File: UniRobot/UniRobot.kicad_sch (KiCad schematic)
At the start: 6 parts, among them J1 Conn_01x01_Socket, J2 Conn_01x01_Socket, Q1 BSS138, U1 RFM69HW

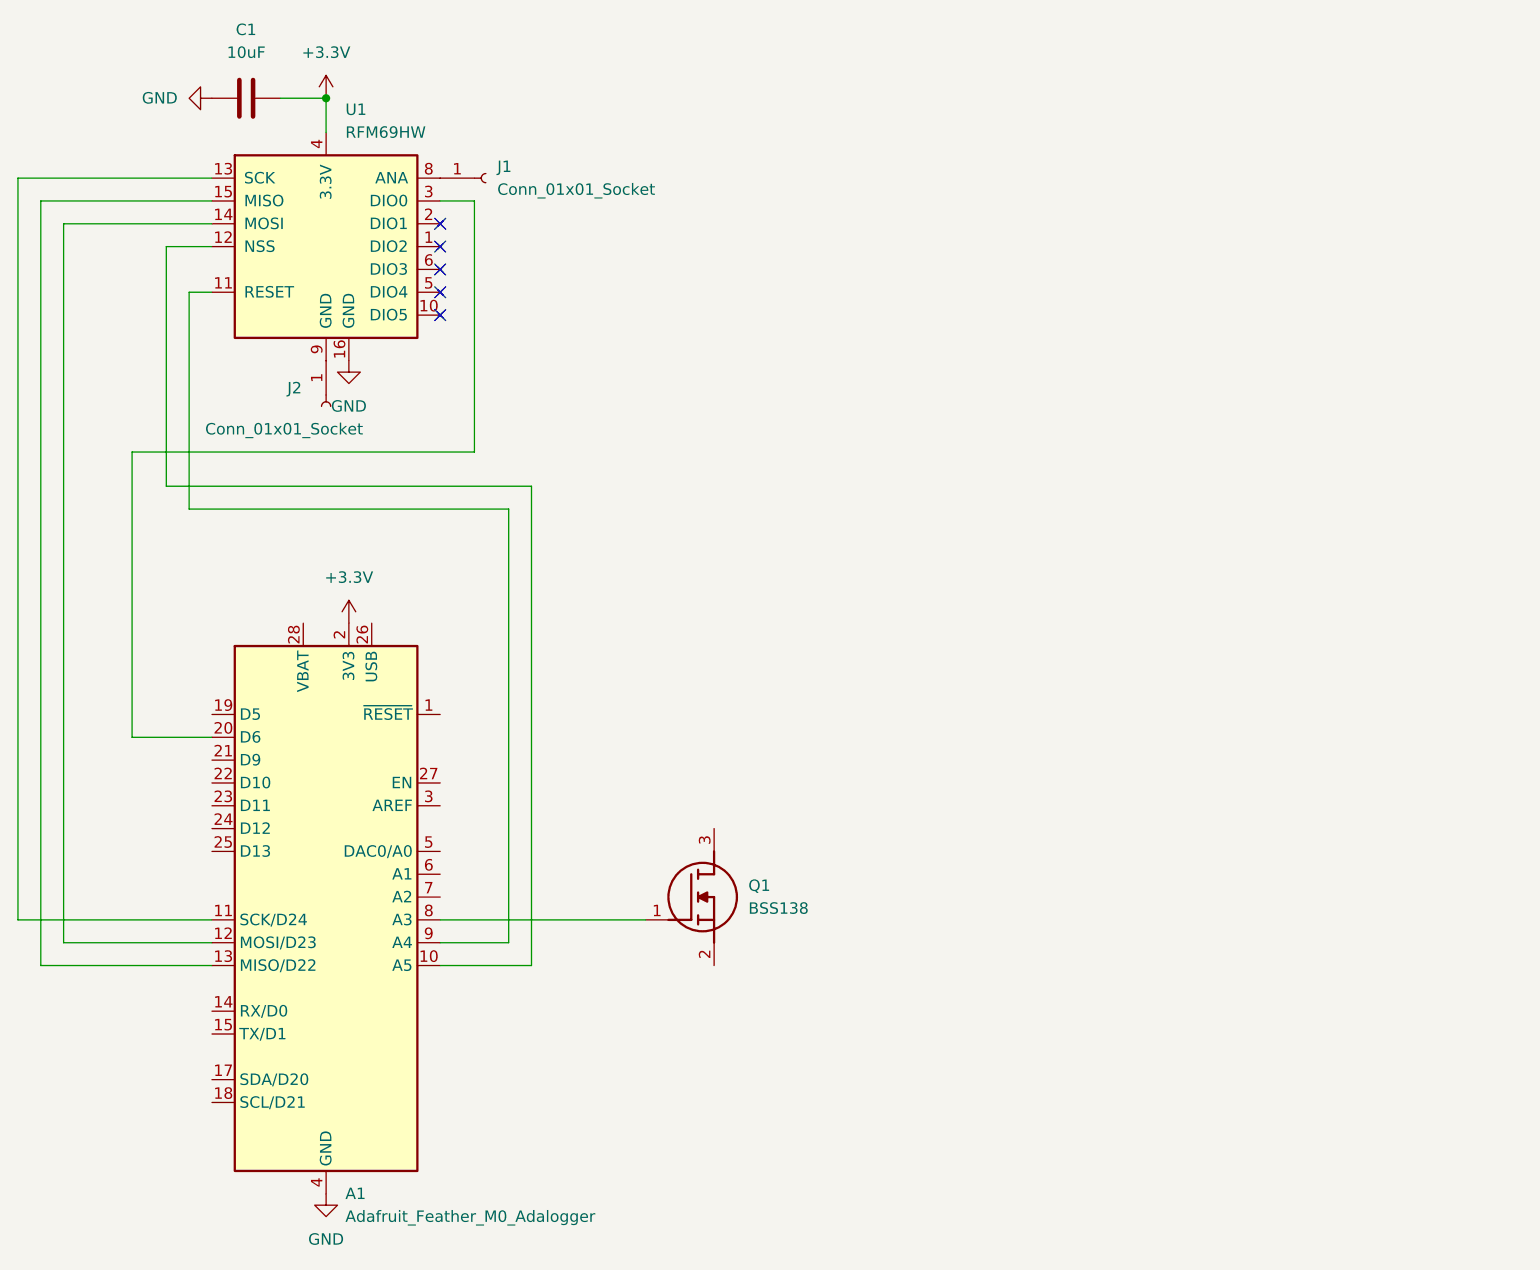
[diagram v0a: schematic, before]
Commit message: lavede robot side pcb.
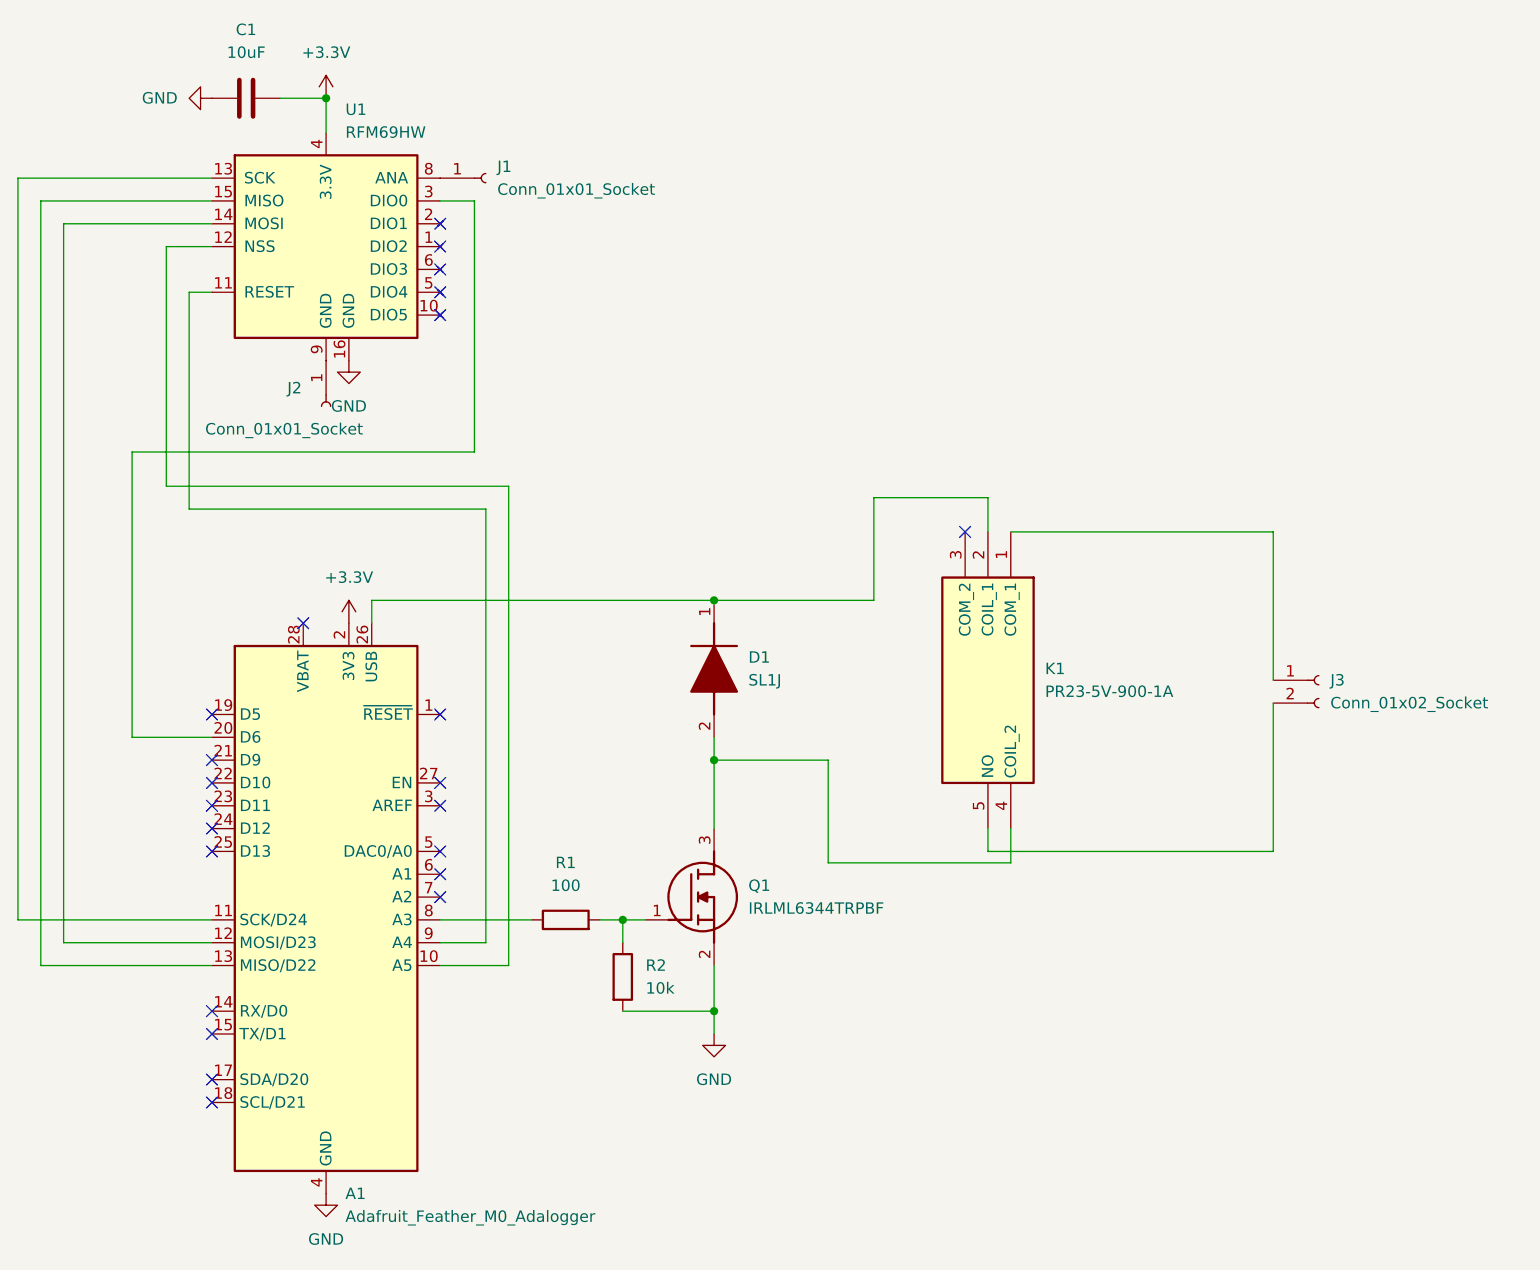
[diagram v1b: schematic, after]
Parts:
- removed Q1: BSS138, SOT95P240X120-3N, symbol Remote-PCB-dele:BSS138
- added D1: SL1J, Remote-footprints:SODFL3718X130N(diode), symbol Remote-PCB-dele:SL1J
- added J3: Conn_01x02_Socket, Connector_PinSocket_2.54mm:PinSocket_1x02_P2.54mm_Vertical, symbol Connector:Conn_01x02_Socket
- added K1: PR23-5V-900-1A, Remote-footprints:PR235V9001A, symbol Remote-PCB-dele:PR23-5V-900-1A
- added Q1: IRLML6344TRPBF, Remote-footprints:SOT95P237X112-3N(nmosTansRelay), symbol Remote-PCB-dele:IRLML6344TRPBF
- added R1: 100, Resistor_SMD:R_0805_2012Metric_Pad1.20x1.40mm_HandSolder, symbol Device:R
- added R2: 10k, Resistor_SMD:R_0805_2012Metric_Pad1.20x1.40mm_HandSolder, symbol Device:R
- C1: footprint (none) -> Capacitor_SMD:C_0805_2012Metric_Pad1.18x1.45mm_HandSolder
- J1, J2: footprint (none) -> Connector_PinSocket_2.54mm:PinSocket_1x01_P2.54mm_Vertical
- U1: footprint RF_Module:HOPERF_RFM69HW -> Remote-footprints:RFM69HCW(homemade)
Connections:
- net GND: now also Q1.2 (S), R2.2
- net at A1.26 (USB): now also D1.1 (K), K1.2 (COIL_1)
- net at A1.8 (A3): now also R1.1
- new net: J3.1 (Pin_1), K1.1 (COM_1)
- new net: J3.2 (Pin_2), K1.5 (NO)
- new net: Q1.1 (G), R1.2, R2.1
- new net: D1.2 (A), K1.4 (COIL_2), Q1.3 (D)
- no-connect marks 5 -> 23

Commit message: Har lavet begge pcber om. Remote har ændret struktur for mere håndholdt design og ekstra knapper plus LEDer. roboside har fået ny relay og LEDer
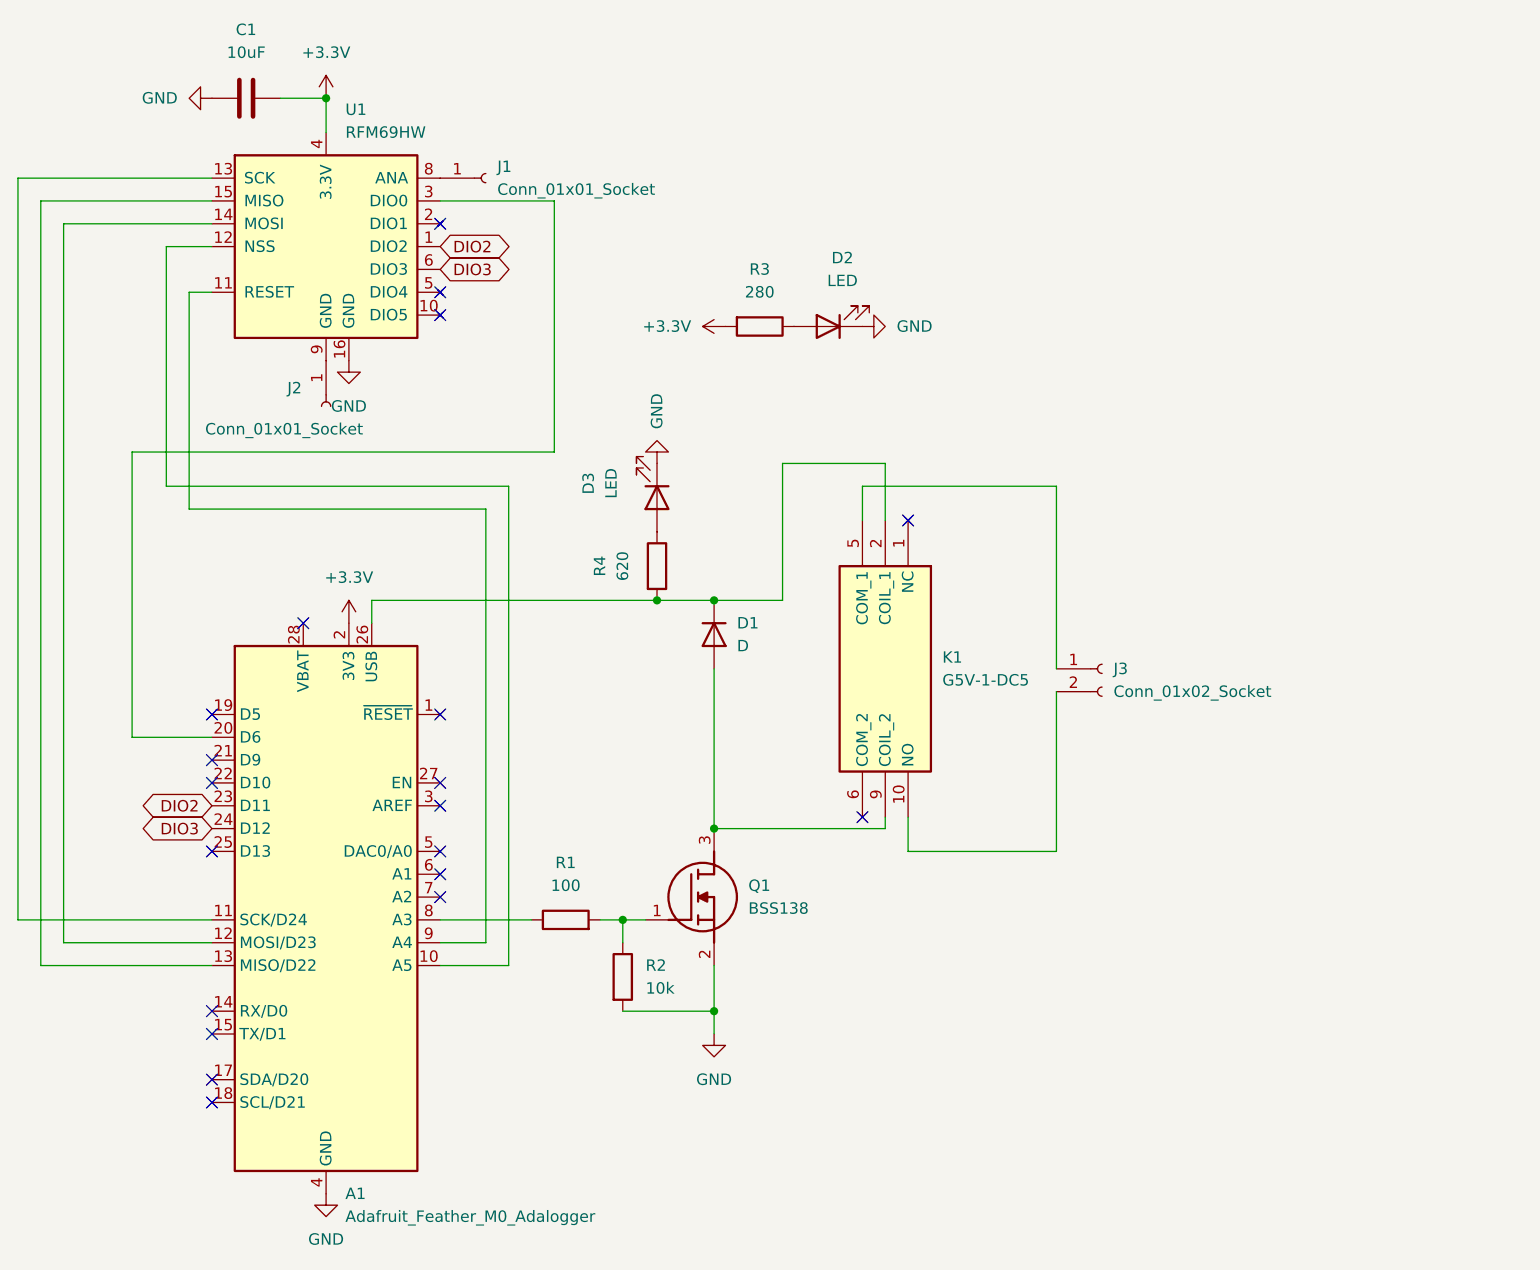
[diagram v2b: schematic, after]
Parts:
- removed D1: SL1J, Remote-footprints:SODFL3718X130N(diode), symbol Remote-PCB-dele:SL1J
- removed K1: PR23-5V-900-1A, Remote-footprints:PR235V9001A, symbol Remote-PCB-dele:PR23-5V-900-1A
- removed Q1: IRLML6344TRPBF, Remote-footprints:SOT95P237X112-3N(nmosTansRelay), symbol Remote-PCB-dele:IRLML6344TRPBF
- added D1: D, Remote-footprints:SODFL3816X120N(diode den vi har), symbol Device:D
- added D2, D3: LED, LED_SMD:LED_0805_2012Metric_Pad1.15x1.40mm_HandSolder, symbol Device:LED
- added K1: G5V-1-DC5, Remote-footprints:G5V1DC24, symbol Remote-PCB-dele:G5V-1-DC5
- added Q1: BSS138, Remote-footprints:nmos, symbol Remote-PCB-dele:BSS138
- added R3: 280, Resistor_SMD:R_0805_2012Metric_Pad1.20x1.40mm_HandSolder, symbol Device:R
- added R4: 620, Resistor_SMD:R_0805_2012Metric_Pad1.20x1.40mm_HandSolder, symbol Device:R
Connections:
- net +3.3V: now also R3.2
- net GND: now also D2.1 (K), D3.1 (K), Q1.2 (S)
- net at J3.1 (Pin_1): now also K1.5 (COM_1)
- net at J3.2 (Pin_2): now also K1.10 (NO)
- net at R1.2, R2.1: now also Q1.1 (G)
- net at A1.26 (USB): now also D1.1 (K), K1.2 (COIL_1), R4.2
- net DIO2: now reaches A1.23 (D11)
- net DIO2: now also U1.1 (DIO2)
- net DIO3: now reaches A1.24 (D12)
- net DIO3: now also U1.6 (DIO3)
- new net: D1.2 (A), K1.9 (COIL_2), Q1.3 (D)
- new net: D3.2 (A), R4.1
- new net: D2.2 (A), R3.1
- no-connect marks 23 -> 20
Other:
- moved on the sheet: J3
